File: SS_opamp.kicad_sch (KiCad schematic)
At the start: 54 parts

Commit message: Final Schematic
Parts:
- UD1, UD2, UD3, UD4, UD5, UD6: footprint (none) -> LMV324AQDRQ1:SOIC127P600X175-14N
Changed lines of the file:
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@@
     (property "Reference" "UD3" (id 0) (at 120.65 48.26 0))
     (property "Value" "LMV324" (id 1) (at 106.68 53.34 0))
-    (property "Footprint" "" (id 2) (at 115.57 50.8 0)
+    (property "Footprint" "LMV324AQDRQ1:SOIC127P600X175-14N" (id 2) (at 115.57 50.8 0)
       (effects (font (size 1.27 1.27)) hide)
     )
@@
       (effects (font (size 1.27 1.27)) (justify left))
     )
-    (property "Footprint" "" (id 2) (at 106.68 156.21 0)
+    (property "Footprint" "LMV324AQDRQ1:SOIC127P600X175-14N" (id 2) (at 106.68 156.21 0)
       (effects (font (size 1.27 1.27)) hide)
     )
@@
     (property "Reference" "UD2" (id 0) (at 74.93 49.53 0))
     (property "Value" "LMV324" (id 1) (at 60.96 53.34 0))
-    (property "Footprint" "" (id 2) (at 69.85 50.8 0)
+    (property "Footprint" "LMV324AQDRQ1:SOIC127P600X175-14N" (id 2) (at 69.85 50.8 0)
       (effects (font (size 1.27 1.27)) hide)
     )
@@
     (property "Reference" "UD2" (id 0) (at 43.18 50.8 0))
     (property "Value" "LMV324" (id 1) (at 27.94 55.88 0))
-    (property "Footprint" "" (id 2) (at 38.1 52.07 0)
+    (property "Footprint" "LMV324AQDRQ1:SOIC127P600X175-14N" (id 2) (at 38.1 52.07 0)
       (effects (font (size 1.27 1.27)) hide)
     )
@@
     (property "Reference" "UD3" (id 0) (at 154.94 26.67 0))
     (property "Value" "LMV324" (id 1) (at 139.7 30.48 0))
-    (property "Footprint" "" (id 2) (at 149.86 27.94 0)
+    (property "Footprint" "LMV324AQDRQ1:SOIC127P600X175-14N" (id 2) (at 149.86 27.94 0)
       (effects (font (size 1.27 1.27)) hide)
     )
@@
     (property "Reference" "UD1" (id 0) (at 66.04 113.03 0))
     (property "Value" "LMV324" (id 1) (at 50.8 118.11 0))
-    (property "Footprint" "" (id 2) (at 60.96 114.3 0)
+    (property "Footprint" "LMV324AQDRQ1:SOIC127P600X175-14N" (id 2) (at 60.96 114.3 0)
       (effects (font (size 1.27 1.27)) hide)
     )
@@
     (property "Reference" "UD3" (id 0) (at 123.19 27.94 0))
     (property "Value" "LMV324" (id 1) (at 109.22 31.75 0))
-    (property "Footprint" "" (id 2) (at 118.11 29.21 0)
+    (property "Footprint" "LMV324AQDRQ1:SOIC127P600X175-14N" (id 2) (at 118.11 29.21 0)
       (effects (font (size 1.27 1.27)) hide)
     )
@@
     (property "Reference" "UD1" (id 0) (at 64.77 88.9 0))
     (property "Value" "LMV324" (id 1) (at 52.07 93.98 0))
-    (property "Footprint" "" (id 2) (at 60.96 90.17 0)
+    (property "Footprint" "LMV324AQDRQ1:SOIC127P600X175-14N" (id 2) (at 60.96 90.17 0)
       (effects (font (size 1.27 1.27)) hide)
     )
@@
       (effects (font (size 1.27 1.27)) (justify left))
     )
-    (property "Footprint" "" (id 2) (at 138.43 157.48 0)
+    (property "Footprint" "LMV324AQDRQ1:SOIC127P600X175-14N" (id 2) (at 138.43 157.48 0)
       (effects (font (size 1.27 1.27)) hide)
     )
@@
     (property "Reference" "UD2" (id 0) (at 68.58 33.02 0))
     (property "Value" "LMV324" (id 1) (at 54.61 35.56 0))
-    (property "Footprint" "" (id 2) (at 63.5 33.02 0)
+    (property "Footprint" "LMV324AQDRQ1:SOIC127P600X175-14N" (id 2) (at 63.5 33.02 0)
       (effects (font (size 1.27 1.27)) hide)
     )
@@
     (property "Reference" "UD4" (id 0) (at 208.28 25.4 0))
     (property "Value" "LMV324" (id 1) (at 195.58 29.21 0))
-    (property "Footprint" "" (id 2) (at 203.2 26.67 0)
+    (property "Footprint" "LMV324AQDRQ1:SOIC127P600X175-14N" (id 2) (at 203.2 26.67 0)
       (effects (font (size 1.27 1.27)) hide)
     )
@@
       (effects (font (size 1.27 1.27)) (justify left))
     )
-    (property "Footprint" "" (id 2) (at 78.74 156.21 0)
+    (property "Footprint" "LMV324AQDRQ1:SOIC127P600X175-14N" (id 2) (at 78.74 156.21 0)
       (effects (font (size 1.27 1.27)) hide)
     )
@@
     (property "Reference" "UD4" (id 0) (at 209.55 45.72 0))
     (property "Value" "LMV324" (id 1) (at 194.31 49.53 0))
-    (property "Footprint" "" (id 2) (at 203.2 46.99 0)
+    (property "Footprint" "LMV324AQDRQ1:SOIC127P600X175-14N" (id 2) (at 203.2 46.99 0)
       (effects (font (size 1.27 1.27)) hide)
     )
@@
     (property "Reference" "UD1" (id 0) (at 36.83 90.17 0))
     (property "Value" "LMV324" (id 1) (at 21.59 95.25 0))
-    (property "Footprint" "" (id 2) (at 31.75 91.44 0)
+    (property "Footprint" "LMV324AQDRQ1:SOIC127P600X175-14N" (id 2) (at 31.75 91.44 0)
       (effects (font (size 1.27 1.27)) hide)
     )
@@
     (property "Reference" "UD6" (id 0) (at 148.59 116.84 0))
     (property "Value" "LMV324" (id 1) (at 134.62 120.65 0))
-    (property "Footprint" "" (id 2) (at 143.51 118.11 0)
+    (property "Footprint" "LMV324AQDRQ1:SOIC127P600X175-14N" (id 2) (at 143.51 118.11 0)
       (effects (font (size 1.27 1.27)) hide)
     )
@@
       (effects (font (size 1.27 1.27)) (justify left))
     )
-    (property "Footprint" "" (id 2) (at 123.19 157.48 0)
+    (property "Footprint" "LMV324AQDRQ1:SOIC127P600X175-14N" (id 2) (at 123.19 157.48 0)
       (effects (font (size 1.27 1.27)) hide)
     )
@@
     (property "Reference" "UD2" (id 0) (at 41.91 31.75 0))
     (property "Value" "LMV324" (id 1) (at 25.4 36.83 0))
-    (property "Footprint" "" (id 2) (at 36.83 33.02 0)
+    (property "Footprint" "LMV324AQDRQ1:SOIC127P600X175-14N" (id 2) (at 36.83 33.02 0)
       (effects (font (size 1.27 1.27)) hide)
     )
@@
       (effects (font (size 1.27 1.27)) (justify left))
     )
-    (property "Footprint" "" (id 2) (at 63.5 153.67 0)
+    (property "Footprint" "LMV324AQDRQ1:SOIC127P600X175-14N" (id 2) (at 63.5 153.67 0)
       (effects (font (size 1.27 1.27)) hide)
     )
@@
     (property "Reference" "UD4" (id 0) (at 243.84 26.67 0))
     (property "Value" "LMV324" (id 1) (at 227.33 30.48 0))
-    (property "Footprint" "" (id 2) (at 237.49 27.94 0)
+    (property "Footprint" "LMV324AQDRQ1:SOIC127P600X175-14N" (id 2) (at 237.49 27.94 0)
       (effects (font (size 1.27 1.27)) hide)
     )
@@
     (property "Reference" "UD6" (id 0) (at 113.03 115.57 0))
     (property "Value" "LMV324" (id 1) (at 100.33 120.65 0))
-    (property "Footprint" "" (id 2) (at 109.22 118.11 0)
+    (property "Footprint" "LMV324AQDRQ1:SOIC127P600X175-14N" (id 2) (at 109.22 118.11 0)
       (effects (font (size 1.27 1.27)) hide)
     )
@@
     (property "Reference" "UD3" (id 0) (at 158.75 48.26 0))
     (property "Value" "LMV324" (id 1) (at 146.05 52.07 0))
-    (property "Footprint" "" (id 2) (at 153.67 49.53 0)
+    (property "Footprint" "LMV324AQDRQ1:SOIC127P600X175-14N" (id 2) (at 153.67 49.53 0)
       (effects (font (size 1.27 1.27)) hide)
     )
@@
     (property "Reference" "UD5" (id 0) (at 214.63 110.49 0))
     (property "Value" "LMV324" (id 1) (at 198.12 116.84 0))
-    (property "Footprint" "" (id 2) (at 209.55 113.03 0)
+    (property "Footprint" "LMV324AQDRQ1:SOIC127P600X175-14N" (id 2) (at 209.55 113.03 0)
       (effects (font (size 1.27 1.27)) hide)
     )
@@
     (property "Reference" "UD5" (id 0) (at 256.54 80.01 0))
     (property "Value" "LMV324" (id 1) (at 241.3 85.09 0))
-    (property "Footprint" "" (id 2) (at 251.46 82.55 0)
+    (property "Footprint" "LMV324AQDRQ1:SOIC127P600X175-14N" (id 2) (at 251.46 82.55 0)
       (effects (font (size 1.27 1.27)) hide)
     )
@@
     (property "Reference" "UD5" (id 0) (at 205.74 81.28 0))
     (property "Value" "LMV324" (id 1) (at 190.5 86.36 0))
-    (property "Footprint" "" (id 2) (at 200.66 82.55 0)
+    (property "Footprint" "LMV324AQDRQ1:SOIC127P600X175-14N" (id 2) (at 200.66 82.55 0)
       (effects (font (size 1.27 1.27)) hide)
     )
@@
     (property "Reference" "UD1" (id 0) (at 31.75 110.49 0))
     (property "Value" "LMV324" (id 1) (at 17.78 115.57 0))
-    (property "Footprint" "" (id 2) (at 26.67 111.76 0)
+    (property "Footprint" "LMV324AQDRQ1:SOIC127P600X175-14N" (id 2) (at 26.67 111.76 0)
       (effects (font (size 1.27 1.27)) hide)
     )
@@
     (property "Reference" "UD4" (id 0) (at 251.46 49.53 0))
     (property "Value" "LMV324" (id 1) (at 238.76 52.07 0))
-    (property "Footprint" "" (id 2) (at 246.38 49.53 0)
+    (property "Footprint" "LMV324AQDRQ1:SOIC127P600X175-14N" (id 2) (at 246.38 49.53 0)
       (effects (font (size 1.27 1.27)) hide)
     )
@@
     (property "Reference" "UD6" (id 0) (at 113.03 83.82 0))
     (property "Value" "LMV324" (id 1) (at 99.06 87.63 0))
-    (property "Footprint" "" (id 2) (at 107.95 85.09 0)
+    (property "Footprint" "LMV324AQDRQ1:SOIC127P600X175-14N" (id 2) (at 107.95 85.09 0)
       (effects (font (size 1.27 1.27)) hide)
     )
@@
       (effects (font (size 1.27 1.27)) (justify left))
     )
-    (property "Footprint" "" (id 2) (at 93.98 154.94 0)
+    (property "Footprint" "LMV324AQDRQ1:SOIC127P600X175-14N" (id 2) (at 93.98 154.94 0)
       (effects (font (size 1.27 1.27)) hide)
     )
@@
     (property "Reference" "UD6" (id 0) (at 154.94 85.09 0))
     (property "Value" "LMV324" (id 1) (at 139.7 87.63 0))
-    (property "Footprint" "" (id 2) (at 149.86 85.09 0)
+    (property "Footprint" "LMV324AQDRQ1:SOIC127P600X175-14N" (id 2) (at 149.86 85.09 0)
       (effects (font (size 1.27 1.27)) hide)
     )
@@
     (property "Reference" "UD5" (id 0) (at 262.89 111.76 0))
     (property "Value" "LMV324" (id 1) (at 248.92 115.57 0))
-    (property "Footprint" "" (id 2) (at 257.81 113.03 0)
-      (effects (font (size 1.27 1.27)) hide)
-    )
+    (property "Footprint" "LMV324AQDRQ1:SOIC127P600X175-14N" (id 2) (at 257.81 113.03 0)
+      (effects (font (size 1.27 1.27)) hide)
+    )

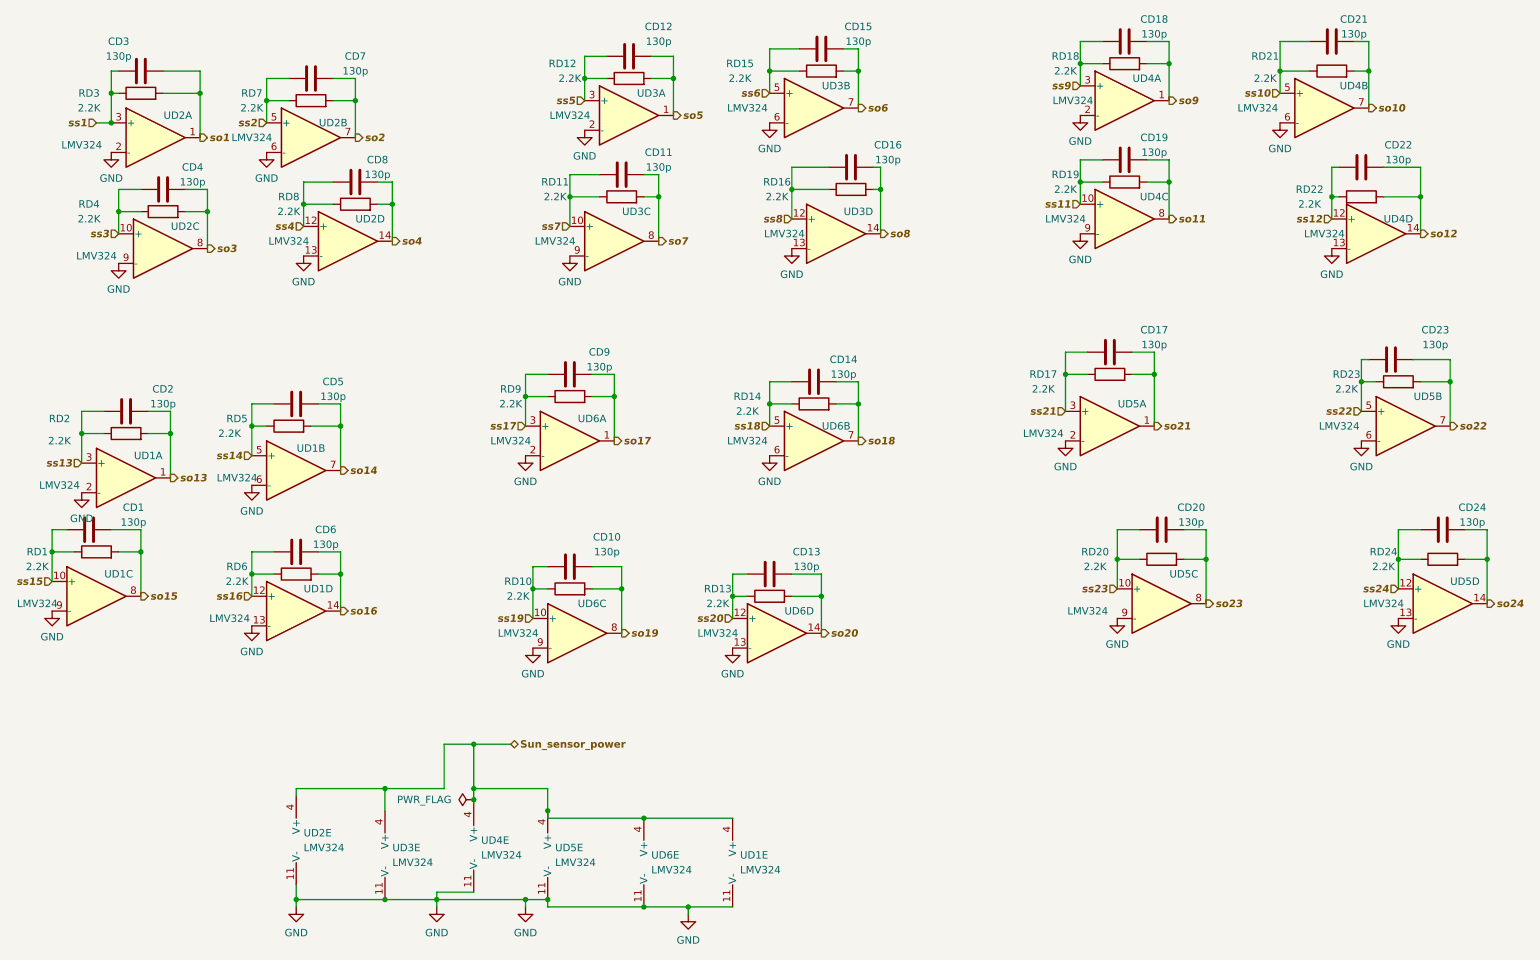
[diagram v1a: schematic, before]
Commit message: MCU circuitry forgot LOL
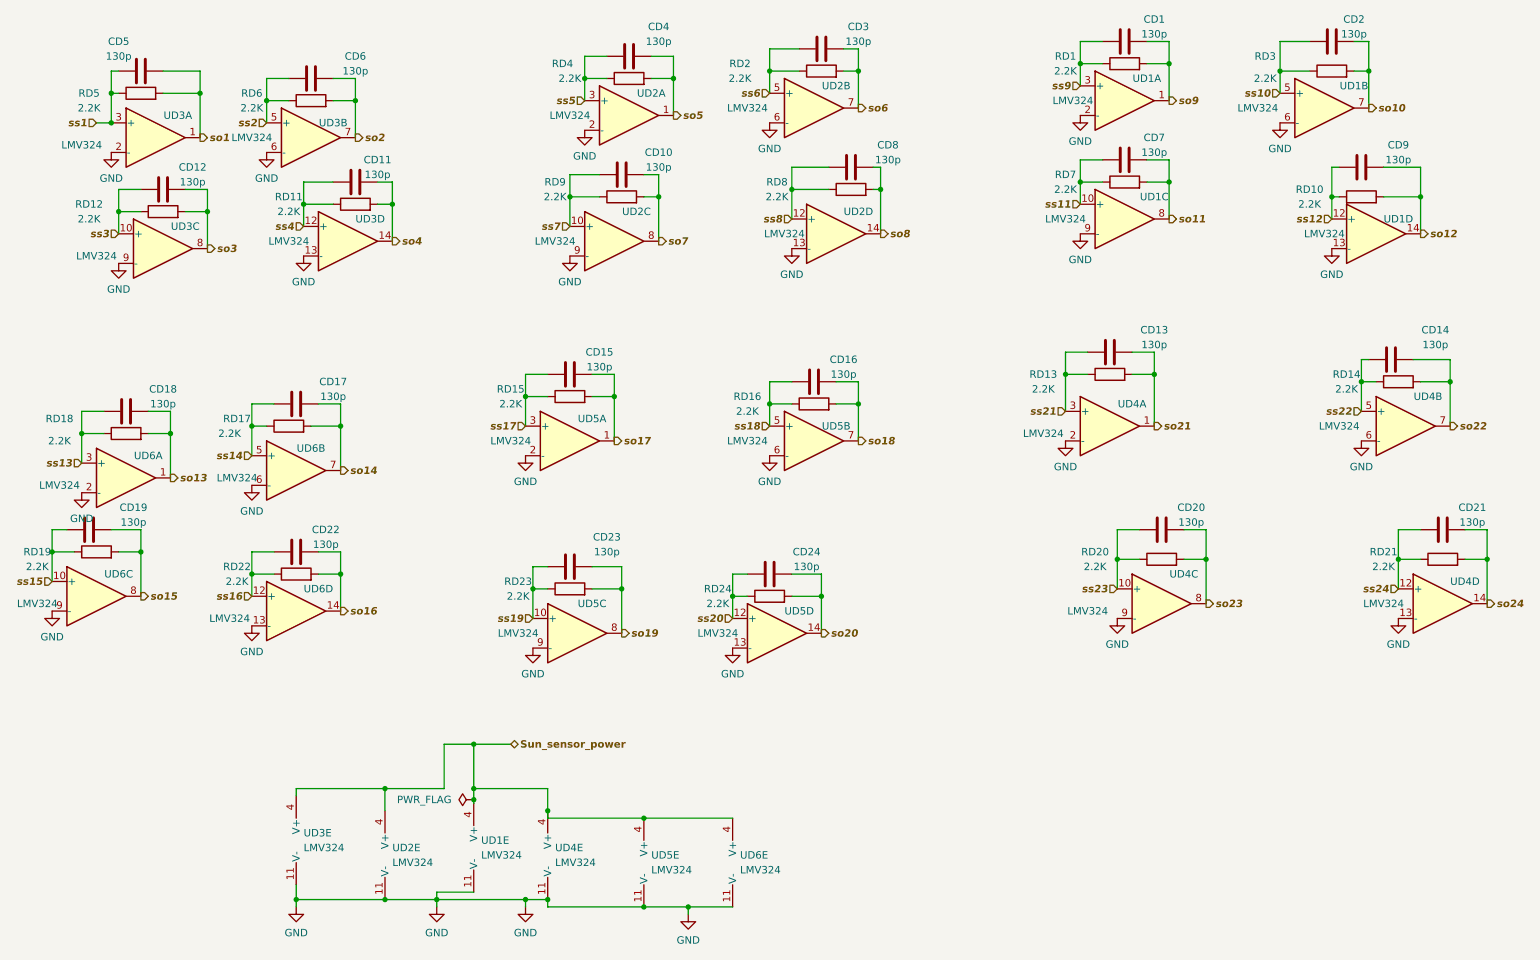
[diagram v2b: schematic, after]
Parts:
- renumbered CD18 to CD1, CD11 to CD10, CD8 to CD11, CD4 to CD12, CD17 to CD13, CD23 to CD14, CD9 to CD15, CD14 to CD16, CD5 to CD17, CD2 to CD18, CD1 to CD19, CD21 to CD2, CD24 to CD21, CD6 to CD22, CD10 to CD23, CD13 to CD24, CD15 to CD3, CD12 to CD4, CD3 to CD5, CD7 to CD6, CD19 to CD7, CD16 to CD8, CD22 to CD9, RD18 to RD1, RD22 to RD10, RD8 to RD11, RD4 to RD12, RD17 to RD13, RD23 to RD14, RD9 to RD15, RD14 to RD16, RD5 to RD17, RD2 to RD18, RD1 to RD19, RD15 to RD2, RD24 to RD21, RD6 to RD22, RD10 to RD23, RD13 to RD24, RD21 to RD3, RD12 to RD4, RD3 to RD5, RD7 to RD6, RD19 to RD7, RD16 to RD8, RD11 to RD9, UD4 to UD1, UD3 to UD2, UD2 to UD3, UD5 to UD4, UD6 to UD5, UD1 to UD6
